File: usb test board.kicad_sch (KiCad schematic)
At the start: 8 parts, among them J1 Conn_01x04_Pin, J2 USB_A, J5 USB_C_Receptacle_USB2.0, J6 USB_B_Micro

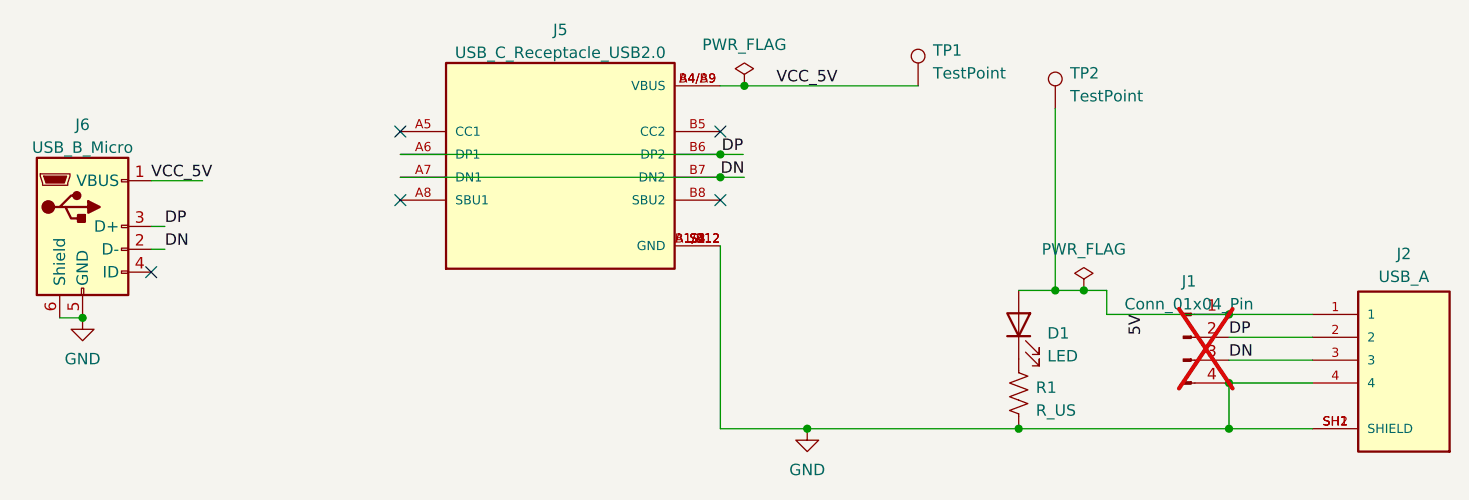
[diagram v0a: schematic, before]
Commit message: correct usb-a data pin polarity
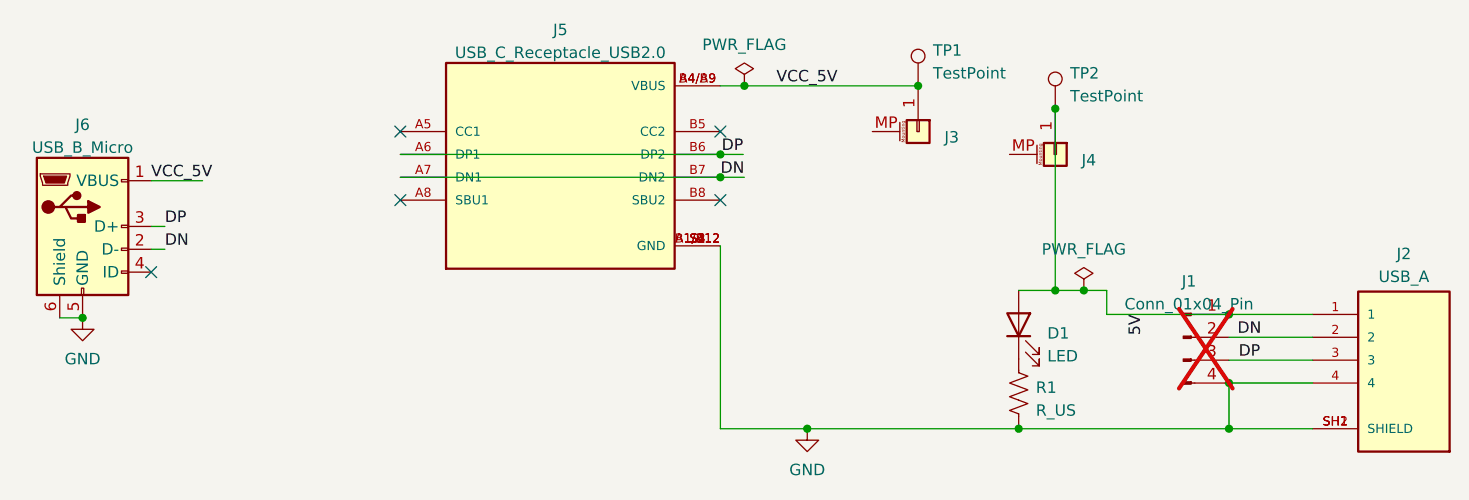
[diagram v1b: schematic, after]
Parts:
- added J3, J4: Conn_01x01_MountingPin, Connector_Pin:Pin_D1.0mm_L10.0mm, symbol Connector_Generic_MountingPin:Conn_01x01_MountingPin
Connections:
- net 5V: now also J4.1 (Pin_1)
- net DN: now also J1.2 (Pin_2), J2.2; no longer J1.3 (Pin_3), J2.3
- net DP: now also J1.3 (Pin_3), J2.3; no longer J1.2 (Pin_2), J2.2
- net VCC_5V: now also J3.1 (Pin_1)
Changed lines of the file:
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@@
   (junction (at 205.613 149.733) (diameter 0) (color 0 0 0 0)
   )
+  (junction (at 186.309 119.253) (diameter 0) (color 0 0 0 0)
+  )
   (junction (at 205.613 154.813) (diameter 0) (color 0 0 0 0)
   )
@@
   )
   (junction (at 205.613 142.113) (diameter 0) (color 0 0 0 0)
+  )
+  (junction (at 171.069 116.713) (diameter 0) (color 0 0 0 0)
   )
   (junction (at 186.309 139.446) (diameter 0) (color 0 0 0 0)
@@
     (stroke (width 0) (type default))
   )
+  (wire (pts (xy 85.852 132.334) (xy 87.376 132.334))
+    (stroke (width 0) (type default))
+  )
+  (wire (pts (xy 149.098 124.333) (xy 151.638 124.333))
+    (stroke (width 0) (type default))
+  )
+  (wire (pts (xy 186.309 119.253) (xy 186.309 139.446))
+    (stroke (width 0) (type default))
+  )
+  (wire (pts (xy 205.613 142.113) (xy 214.884 142.113))
+    (stroke (width 0) (type default))
+  )
+  (wire (pts (xy 149.098 154.813) (xy 158.75 154.813))
+    (stroke (width 0) (type default))
+  )
+  (wire (pts (xy 85.852 134.874) (xy 87.376 134.874))
+    (stroke (width 0) (type default))
+  )
+  (wire (pts (xy 205.613 149.733) (xy 205.613 154.813))
+    (stroke (width 0) (type default))
+  )
   (wire (pts (xy 205.613 144.653) (xy 214.884 144.653))
-    (stroke (width 0) (type default))
-  )
-  (wire (pts (xy 85.852 132.334) (xy 87.376 132.334))
-    (stroke (width 0) (type default))
-  )
-  (wire (pts (xy 149.098 124.333) (xy 151.638 124.333))
-    (stroke (width 0) (type default))
-  )
-  (wire (pts (xy 186.309 119.253) (xy 186.309 139.446))
-    (stroke (width 0) (type default))
-  )
-  (wire (pts (xy 205.613 142.113) (xy 214.884 142.113))
-    (stroke (width 0) (type default))
-  )
-  (wire (pts (xy 149.098 154.813) (xy 158.75 154.813))
-    (stroke (width 0) (type default))
-  )
-  (wire (pts (xy 85.852 134.874) (xy 87.376 134.874))
-    (stroke (width 0) (type default))
-  )
-  (wire (pts (xy 205.613 149.733) (xy 205.613 154.813))
     (stroke (width 0) (type default))
   )
@@
     (effects (font (size 1.27 1.27)) (justify right bottom))
   )
+  (label "DP" (at 206.6798 147.193 0) (fields_autoplaced)
+    (effects (font (size 1.27 1.27)) (justify left bottom))
+  )
+  (label "DN" (at 206.5528 144.653 0) (fields_autoplaced)
+    (effects (font (size 1.27 1.27)) (justify left bottom))
+  )
   (label "5V" (at 196.215 142.113 270) (fields_autoplaced)
     (effects (font (size 1.27 1.27)) (justify right bottom))
@@
     (effects (font (size 1.27 1.27)) (justify left bottom))
   )
-  (label "DP" (at 205.613 144.653 0) (fields_autoplaced)
-    (effects (font (size 1.27 1.27)) (justify left bottom))
-  )
-  (label "DN" (at 205.613 147.193 0) (fields_autoplaced)
-    (effects (font (size 1.27 1.27)) (justify left bottom))
-  )
   (label "DP" (at 87.376 132.334 0) (fields_autoplaced)
     (effects (font (size 1.27 1.27)) (justify left bottom))
+  )
+  (symbol (lib_id "Connector_Generic_MountingPin:Conn_01x01_MountingPin") (at 171.069 121.793 270) (unit 1)
+    (in_bom yes) (on_board yes) (dnp no) (fields_autoplaced)
+    (property "Reference" "J3" (at 173.99 122.428 90)
+      (effects (font (size 1.27 1.27)) (justify left))
+    )
+    (property "Value" "Conn_01x01_MountingPin" (at 173.99 123.698 90)
+      (effects (font (size 1.27 1.27)) (justify left) hide)
+    )
+    (property "Footprint" "Connector_Pin:Pin_D1.0mm_L10.0mm" (at 171.069 121.793 0)
+      (effects (font (size 1.27 1.27)) hide)
+    )
+    (property "Datasheet" "~" (at 171.069 121.793 0)
+      (effects (font (size 1.27 1.27)) hide)
+    )
+    (pin "1")
+    (pin "MP")
+    (instances
+      (project "usb test board"
+        (path "/8f52a1f3-af29-4f09-ad4b-07320ea77f78"
+          (reference "J3") (unit 1)
+        )
+      )
+    )
   )
   (symbol (lib_id "USB4110GFA:USB4110GFA") (at 131.318 124.333 0) (unit 1)
@@
         )
       )
+    )
+  )
+  (symbol (lib_id "Connector_Generic_MountingPin:Conn_01x01_MountingPin") (at 186.309 124.333 270) (unit 1)
+    (in_bom yes) (on_board yes) (dnp no) (fields_autoplaced)
+    (property "Reference" "J4" (at 189.23 124.968 90)
+      (effects (font (size 1.27 1.27)) (justify left))
+    )
+    (property "Value" "Conn_01x01_MountingPin" (at 189.23 126.238 90)
+      (effects (font (size 1.27 1.27)) (justify left) hide)
+    )
+    (property "Footprint" "Connector_Pin:Pin_D1.0mm_L10.0mm" (at 186.309 124.333 0)
+      (effects (font (size 1.27 1.27)) hide)
+    )
+    (property "Datasheet" "~" (at 186.309 124.333 0)
+      (effects (font (size 1.27 1.27)) hide)
+    )
+    (pin "1")
+    (pin "MP")
+    (instances
+      (project "usb test board"
+        (path "/8f52a1f3-af29-4f09-ad4b-07320ea77f78"
+          (reference "J4") (unit 1)
+        )
+      )
